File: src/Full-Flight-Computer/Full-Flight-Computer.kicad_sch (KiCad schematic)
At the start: 40 parts, among them J1 Jumper_NO, J2 Jumper_NO, P1 647676-2, P2 1546551-2, P3 3220-20-0200-00, U1 STM32H750VBTx, U2 LMS8117AMP-3.3_NOPB, Y1 ECS-240-18-33-JGN-TR

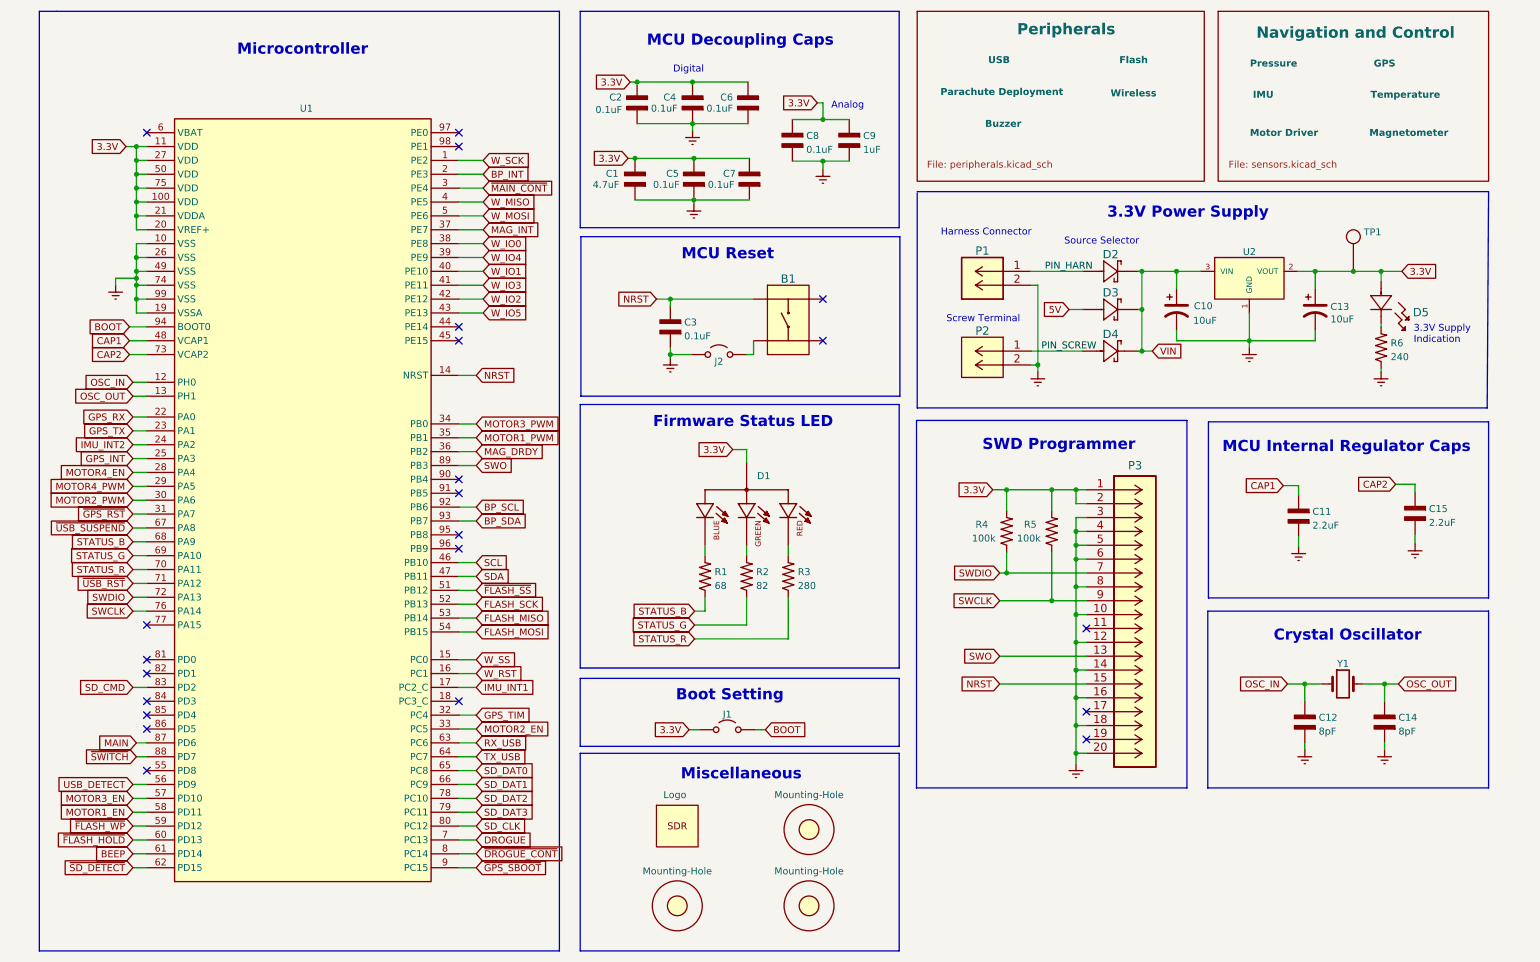
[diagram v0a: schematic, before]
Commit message: removed extra sections from schematic
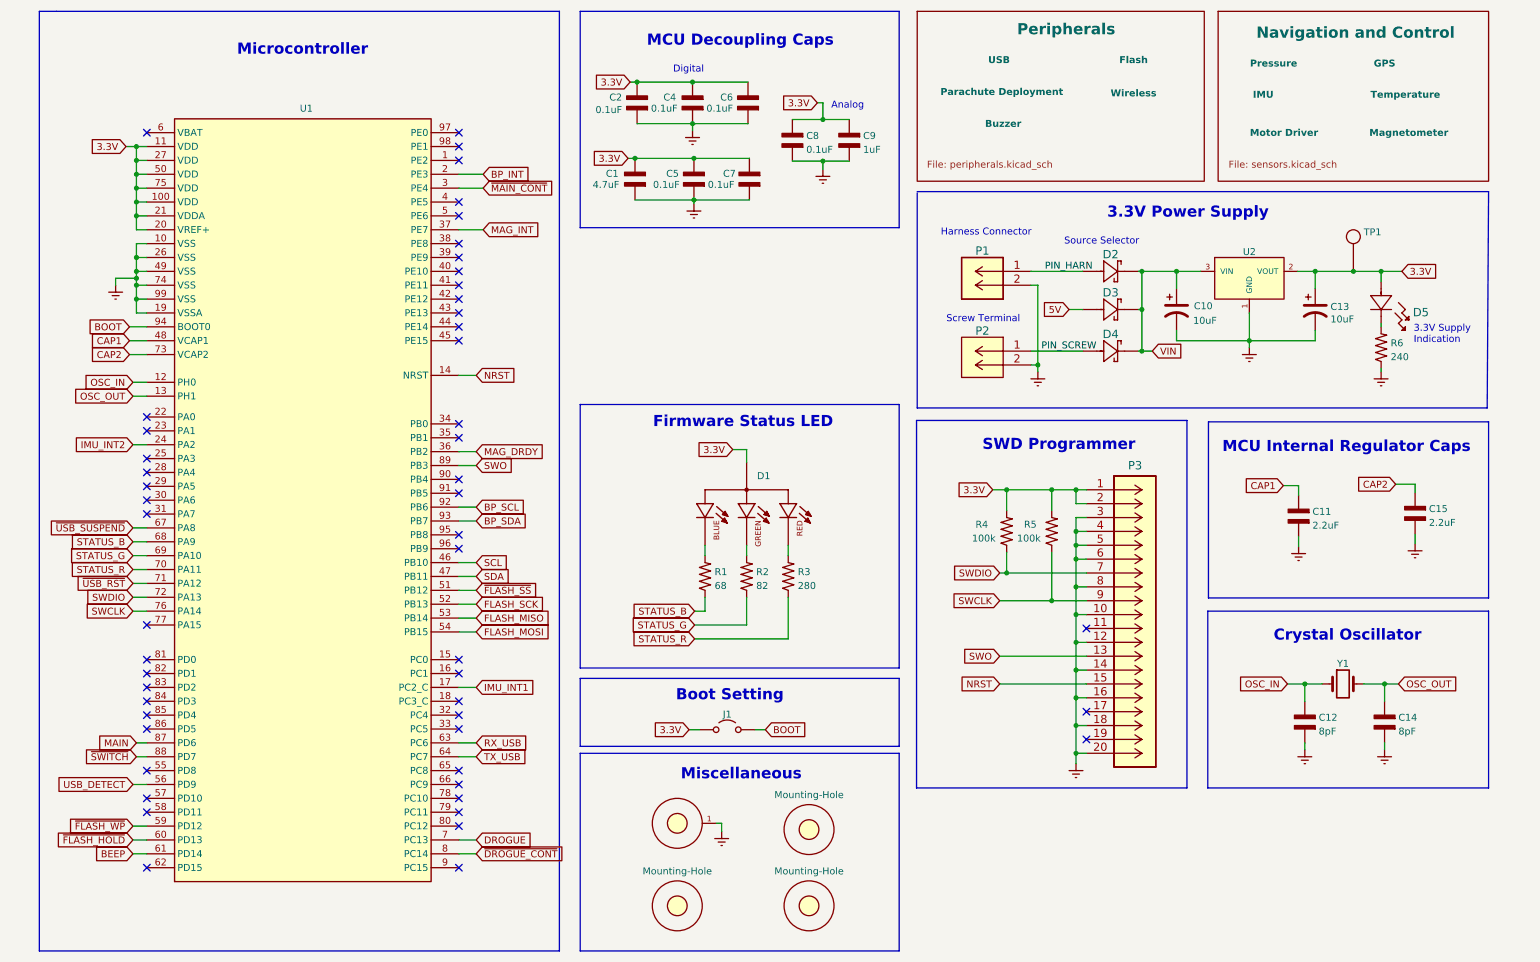
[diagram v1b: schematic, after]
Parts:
- removed B1: PTS647SM38SMTR2LFS, Flight-Computer:PTS647SM38SMTR2LFS, symbol Flight-Computer:PTS647SM38SMTR2LFS
- removed C3: 0.1uF, Flight-Computer:CAP_0603, symbol Flight-Computer:CAP_0603
- removed J2: Jumper_NO, Engine-Controller:Jumper-NO, symbol Flight-Computer:Jumper_NO
- removed LOGO1: Logo, Flight-Computer:Logo, symbol Flight-Computer:Logo
- added H4: Mounting-Hole-4-40, Full-Flight-Computer:MountingHole_4-40, symbol Full-Flight-Computer:Mounting-Hole-4-40
- C1, C2, C4, C5, C6, C8, C9: footprint Flight-Computer:CAP_0603 -> Full-Flight-Computer:CAP_0402; symbol Flight-Computer:CAP_0603 -> Full-Flight-Computer:CAP_0402
- C7: footprint Flight-Computer:CAP_0603 -> Full-Flight-Computer:CAP_0603; symbol Flight-Computer:CAP_0603 -> Full-Flight-Computer:CAP_0603
- U1: footprint Flight-Computer:STM32H750VBT6 -> Full-Flight-Computer:STM32H750VBT6; symbol Flight-Computer:STM32H750VBTx -> Full-Flight-Computer:STM32H750VBTx
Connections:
- net Earth: now also H4.1
- net GPS_INT: no longer names the net of U1.25 (PA3)
- net GPS_RX: no longer names the net of U1.22 (PA0)
- net GPS_TIM: no longer names the net of U1.32 (PC4)
- net GPS_TX: no longer names the net of U1.23 (PA1)
- net MOTOR1_EN: no longer names the net of U1.58 (PD11)
- net MOTOR1_PWM: no longer names the net of U1.35 (PB1)
- net MOTOR2_EN: no longer names the net of U1.33 (PC5)
- net MOTOR2_PWM: no longer names the net of U1.30 (PA6)
- net MOTOR3_EN: no longer names the net of U1.57 (PD10)
- net MOTOR3_PWM: no longer names the net of U1.34 (PB0)
- net MOTOR4_EN: no longer names the net of U1.28 (PA4)
- net MOTOR4_PWM: no longer names the net of U1.29 (PA5)
- net SD_CLK: no longer names the net of U1.80 (PC12)
- net SD_CMD: no longer names the net of U1.83 (PD2)
- net SD_DAT0: no longer names the net of U1.65 (PC8)
- net SD_DAT1: no longer names the net of U1.66 (PC9)
- net SD_DAT2: no longer names the net of U1.78 (PC10)
- net SD_DAT3: no longer names the net of U1.79 (PC11)
- net W_IO0: no longer names the net of U1.38 (PE8)
- net W_IO1: no longer names the net of U1.40 (PE10)
- net W_IO2: no longer names the net of U1.42 (PE12)
- net W_IO3: no longer names the net of U1.41 (PE11)
- net W_IO4: no longer names the net of U1.39 (PE9)
- net W_IO5: no longer names the net of U1.43 (PE13)
- net W_MISO: no longer names the net of U1.4 (PE5)
- net W_MOSI: no longer names the net of U1.5 (PE6)
- net W_RST: no longer names the net of U1.16 (PC1)
- net W_SCK: no longer names the net of U1.1 (PE2)
- net W_SS: no longer names the net of U1.15 (PC0)
- net ~{GPS_RST}: no longer names the net of U1.31 (PA7)
- net ~{GPS_SBOOT}: no longer names the net of U1.9 (PC15)
- net ~{SD_DETECT}: no longer names the net of U1.62 (PD15)
- no-connect marks 22 -> 52
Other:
- note removed: "MCU Reset"

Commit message: fixed all schematic symbol links to link to correct lib file
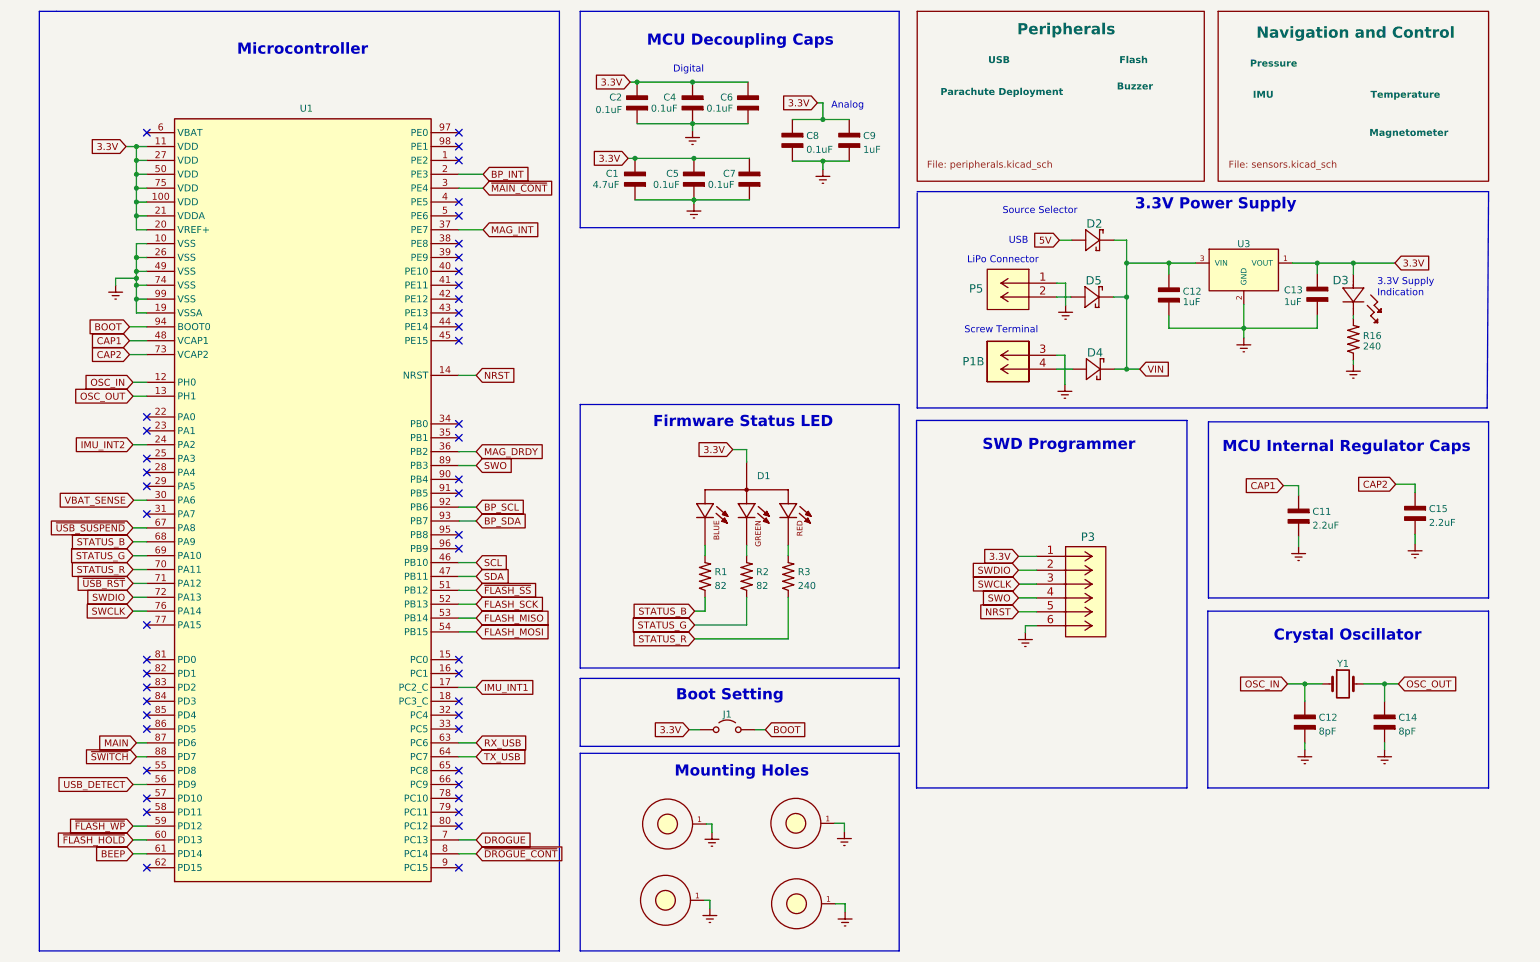
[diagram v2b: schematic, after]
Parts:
- removed C10, C13: 10uF, Flight-Computer:T491A106K010AT, symbol Flight-Computer:CAP_Polar
- removed D2, D3, D4: SM5819PL-TP, Flight-Computer:SM5819PL-TP, symbol Flight-Computer:SM5819PL-TP
- removed D5: SML-LX1206GC-TR, Flight-Computer:SML-LX1206GC-TR, symbol Flight-Computer:SML-LX1206GC-TR
- removed H1, H3: Mounting-Hole, Flight-Computer:MountingHole_3mm, symbol Flight-Computer:Mounting-Hole
- removed P1: 647676-2, Flight-Computer:647676-2, symbol Flight-Computer:647676-2
- removed P2: 1546551-2, Flight-Computer:1546551-2, symbol Flight-Computer:1546551-2
- removed P3: 3220-20-0200-00, Flight-Computer:3220-20-0200-00, symbol Flight-Computer:3220-20-0200-00
- removed R4, R5: 100k, Flight-Computer:RES_0603, symbol Flight-Computer:RES_0603
- removed R6: 240, Flight-Computer:RES_0603, symbol Flight-Computer:RES_0603
- removed TP1: TP, Flight-Computer:TP, symbol Flight-Computer:TP
- removed U2: LMS8117AMP-3.3_NOPB, Flight-Computer:LMS8117AMP-3.3NOPB, symbol Flight-Computer:LMS8117AMP-3.3_NOPB
- added C12, C13: 1uF, Full-Flight-Computer:CAP_0603, symbol Full-Flight-Computer:CAP_0603
- added D2, D4, D5: PMEG3010AESBYL, Full-Flight-Computer:PMEG3010AESBYL, symbol Full-Flight-Computer:PMEG3010AESBYL
- added D3: LTST-C191KGKT, Full-Flight-Computer:LTST-C191KGKT, symbol Full-Flight-Computer:LTST-C191KGKT
- added H1: Mounting-Hole-4-40, Full-Flight-Computer:MountingHole_4-40, symbol Full-Flight-Computer:Mounting-Hole-4-40
- added H3: Mounting-Hole, Full-Flight-Computer:MountingHole_4-40, symbol Full-Flight-Computer:Mounting-Hole-4-40
- added P1: 1984659, Full-Flight-Computer:1546551-4, symbol Full-Flight-Computer:1546551-4
- added P3: 0530470610, Full-Flight-Computer:53047-0610, symbol Full-Flight-Computer:0530470610
- added P5: B2B-PH-K-SLFSN_JST, Full-Flight-Computer:B2B-PH-K-SLFSN_JST, symbol Full-Flight-Computer:B2B-PH-K-SLFSN_JST
- added R16: 240, Full-Flight-Computer:RES_0402, symbol Full-Flight-Computer:RES_0402
- added U3: LMS8117AMP-3.3_NOPB, Full-Flight-Computer:AP7370-33Y-13, symbol Full-Flight-Computer:AP7370-33Y-13
- C11, C12, C14, C15: footprint Flight-Computer:CAP_0603 -> Full-Flight-Computer:CAP_0402; symbol Flight-Computer:CAP_0603 -> Full-Flight-Computer:CAP_0402
- D1: footprint Flight-Computer:CLMVC-FKA-CL1D1L71BB7C3C3 -> Full-Flight-Computer:CLMVC-FKA-CL1D1L71BB7C3C3; symbol Flight-Computer:CLMVC-FKA-CL1D1L71BB7C3C3 -> Full-Flight-Computer:CLMVC-FKA-CL1D1L71BB7C3C3
- H2: footprint Flight-Computer:MountingHole_3mm -> Full-Flight-Computer:MountingHole_4-40; symbol Flight-Computer:Mounting-Hole -> Full-Flight-Computer:Mounting-Hole-4-40
- J1: footprint Flight-Computer:Jumper-NO -> Base-Flight-Computer:Jumper-NO; symbol Flight-Computer:Jumper_NO -> Full-Flight-Computer:Jumper_NO
- R1: value 68 -> 82; footprint Flight-Computer:RES_0603 -> Full-Flight-Computer:RES_0402; symbol Flight-Computer:RES_0603 -> Full-Flight-Computer:RES_0402
- R3: value 280 -> 240; footprint Flight-Computer:RES_0603 -> Full-Flight-Computer:RES_0402; symbol Flight-Computer:RES_0603 -> Full-Flight-Computer:RES_0402
- Y1: footprint Flight-Computer:ECS-240-18-33-JGN-TR -> Full-Flight-Computer:ECS-240-12-37B-CKY-TR; symbol Flight-Computer:ECS-240-18-33-JGN-TR -> Full-Flight-Computer:ECS-240-12-37B-CKY-TR
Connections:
- net 3.3V: now also C13.1, D3.2, P3.1, U3.1 (VOUT)
- net 5V: now also D2.A
- net Earth: now also H2.1, C12.2, C13.2, H1.1, H3.1, P1.3 (5), P3.6, P5.1 (5), R16.1, U3.2 (GND)
- net NRST: now also P3.5
- net SWCLK: now also P3.3
- net SWDIO: now also P3.2
- net SWO: now also P3.4
- net VIN: now also C12.1, D2.C, D4.C, D5.C, U3.3 (VIN)
- net VBAT_SENSE: now reaches U1.30 (PA6)
- new net: D5.A, P5.2 (6)
- new net: D3.1, R16.2
- new net: D4.A, P1.4 (6)
- no-connect marks 52 -> 48
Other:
- note added: "LiPo Connector"
- note added: "Mounting Holes"
- note added: "USB"
- note removed: "Harness Connector"
- note removed: "Miscellaneous"

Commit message: added auxiliary ports for staging/redundant ejection charges
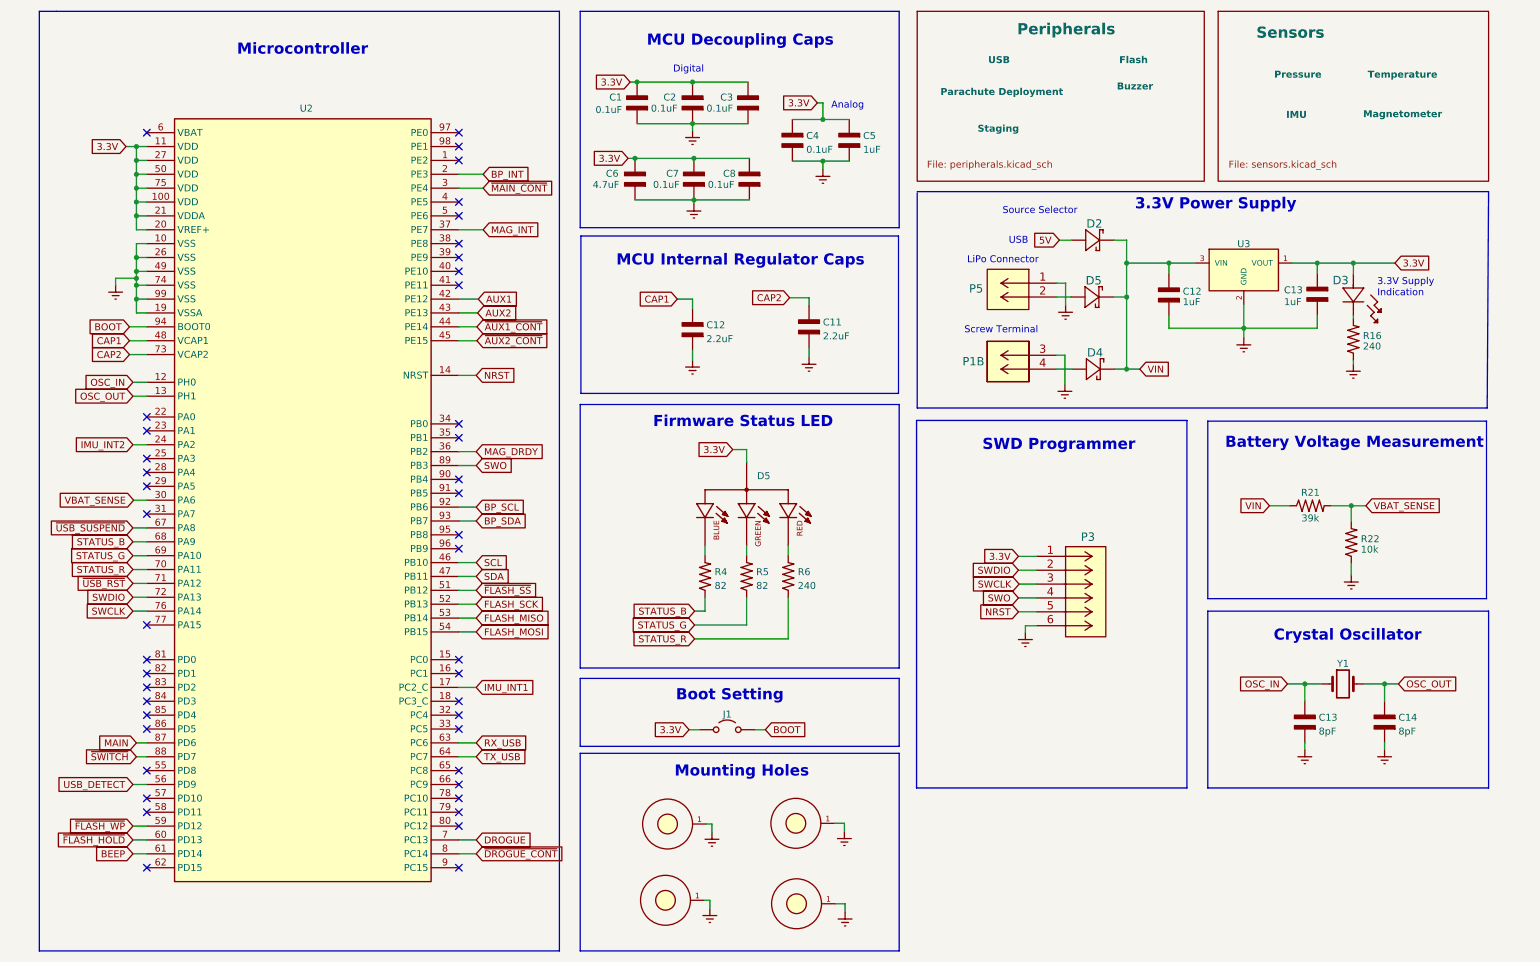
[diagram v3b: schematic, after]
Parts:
- added R21: 39k, Full-Flight-Computer:RES_0402, symbol Full-Flight-Computer:RES_0402
- added R22: 10k, Full-Flight-Computer:RES_0402, symbol Full-Flight-Computer:RES_0402
- renumbered C2 to C1, C15 to C11, C11 to C12, C12 to C13, C4 to C2, C6 to C3, C8 to C4, C9 to C5, C1 to C6, C5 to C7, C7 to C8, D1 to D5, H2 to H1, H4 to H2, H1 to H3, H3 to H4, R1 to R4, R2 to R5, R3 to R6, U1 to U2
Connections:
- net Earth: now also R22.1
- net VBAT_SENSE: now also R21.2, R22.2
- net VIN: now also R21.1
- net AUX1: now reaches U2.42 (PE12)
- net AUX2: now reaches U2.43 (PE13)
- net ~{AUX1_CONT}: now reaches U2.44 (PE14)
- net ~{AUX2_CONT}: now reaches U2.45 (PE15)
- no-connect marks 48 -> 44
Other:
- sheet Navigation and Control renamed Sensors
- note added: "Battery Voltage Measurement"
- moved on the sheet: C11, C12
